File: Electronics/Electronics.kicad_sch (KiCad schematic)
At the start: 20 parts, among them J1 Barrel_Jack, M1 Fan_4pin, Q1 PN2222A, Q2 PN2222A, Q3 PN2222A, SW1 MOTOR_DECREASE, SW2 MOTOR_INCREASE, SW3 CYCLE_COLOR, SW4 CYCLE_MODE, U1 ESP32-DevKitC

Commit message: Updated schematic. Working on footprints. Need to add new DevKit Symbol to schematic
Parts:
- removed U1: ESP32-DevKitC, PCM_Espressif:ESP32-DevKitC, symbol PCM_Espressif:ESP32-DevKitC
- added R10, R11: 10K, symbol Device:R
- added R9: 100, symbol Device:R
- added SW5: SW_Wuerth_450301014042, Button_Switch_THT:SW_Slide-03_Wuerth-WS-SLTV_10x2.5x6.4_P2.54mm, symbol Switch:SW_Wuerth_450301014042
- added U1: ~, symbol Custom_Symbols:ESP-32S-Dev-Board
- added U3: ESP32-DEVKIT-V1, ESP32-DEVKIT-V1:MODULE_ESP32_DEVKIT_V1, symbol ESP_DEVKITV1:ESP32-DEVKIT-V1
- D1: footprint (none) -> Connector:FanPinHeader_1x04_P2.54mm_Vertical
- D2: footprint (none) -> LED_THT:LED_D5.0mm
- J1: footprint Connector_BarrelJack:BarrelJack_SwitchcraftConxall_RAPC10U_Horizontal -> Connector_BarrelJack:BarrelJack_Wuerth_6941xx301002
- SW1, SW2, SW3, SW4: footprint (none) -> Button_Switch_THT:SW_PUSH_6mm
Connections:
- net GND: now also R9.2; no longer D2.1 (K), Q1.1 (E), Q2.1 (E), Q3.1 (E), U2.4 (GND)
- net at SW1.1, SW2.1, SW3.1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: now also U1.15 (Vin)
- net at SW2.4 (A): now also U1.7 (D33)
- net at D1.1 (A), M1.2 (+): now also SW5.3 (A); no longer U2.1 (VIN)
- net at R7.2: now also U1.19 (D2)
- net at D1.3 (RK): now also Q3.3 (C); no longer Q1.3 (C)
- net at D1.4 (BK): now also Q1.3 (C); no longer Q3.3 (C)
- net at R5.2: now also U1.23 (D5)
- net at R6.2: now also U1.20 (D4)
- net at SW3.3 (K): now also U1.4 (D34)
- net at SW4.4 (A): now also U1.5 (D35)
- net at SW1.3 (K): now also U1.6 (D32)
- new net: D2.1 (K), R9.1
- new net: R10.1, R11.1, U1.14 (gnd), U2.4 (GND)
- new net: R11.2, U1.3 (VN)
- new net: SW5.2 (C), U2.1 (VIN)
- new net: R10.2, U1.2 (VP)
- new net: U3.2 (GND), U3.29 (GND)
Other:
- moved on the sheet: D2, R1, R2, R3, R4, SW1, SW2, SW3, SW4

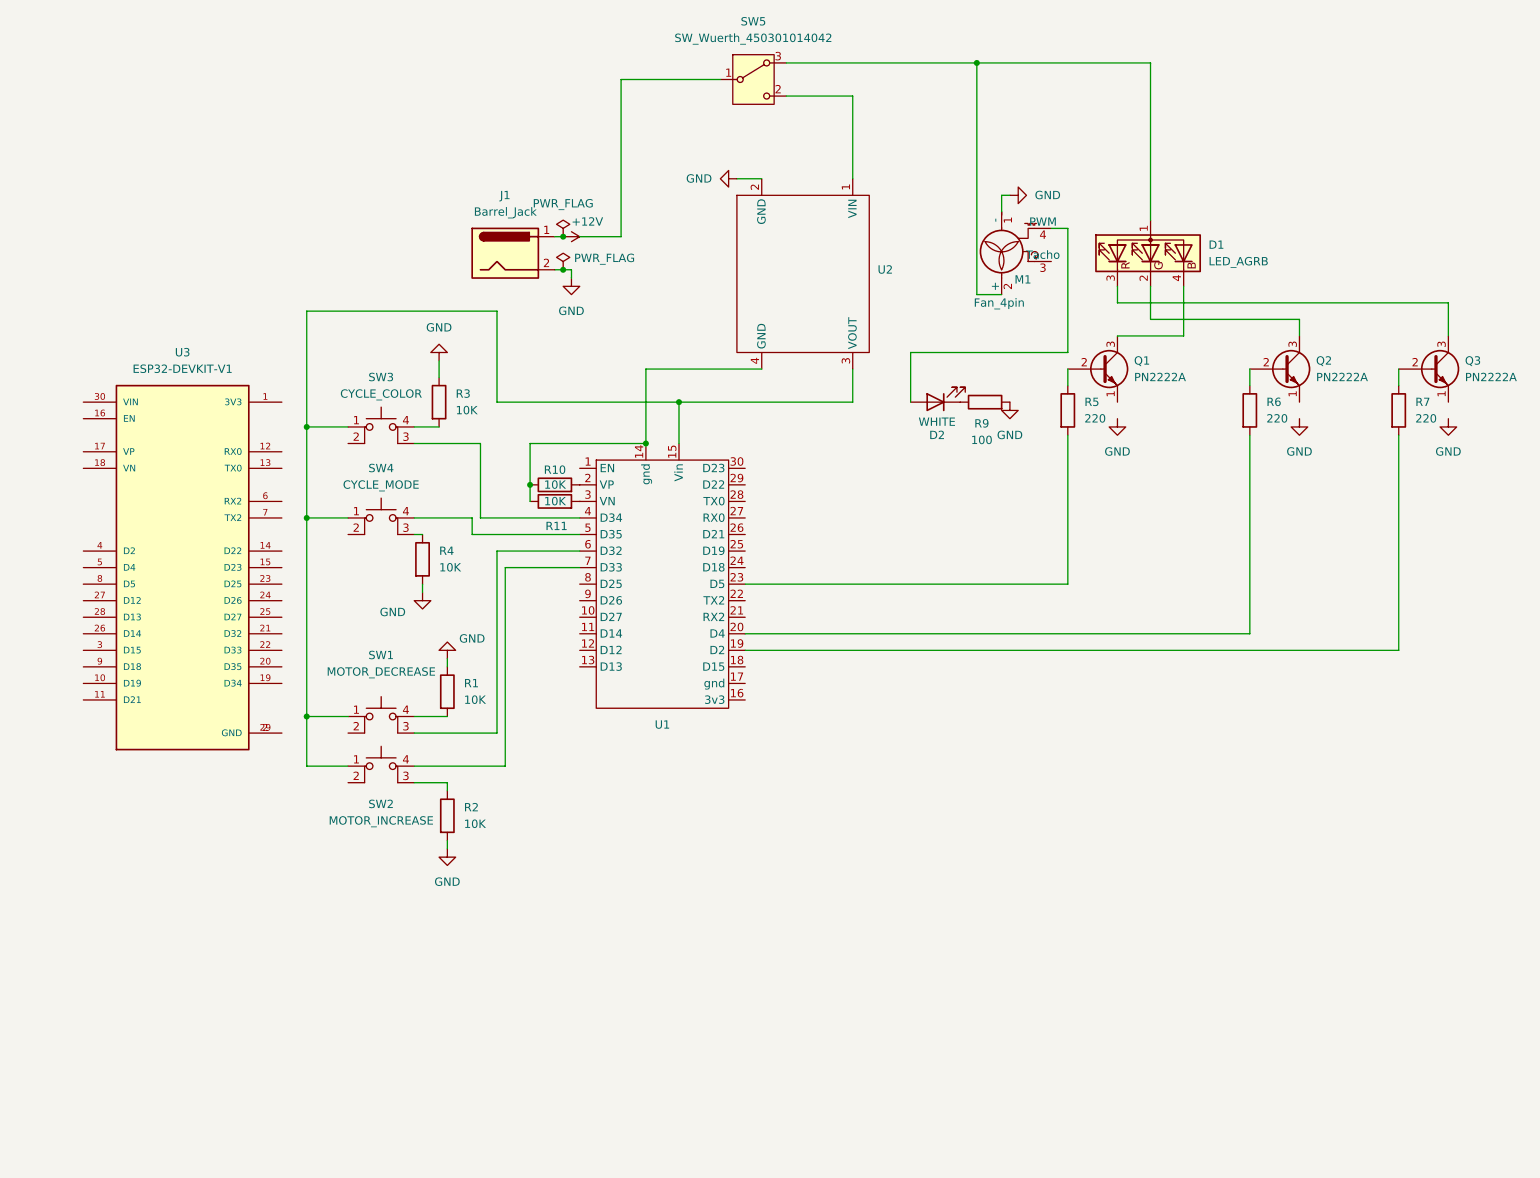
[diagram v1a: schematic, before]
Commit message: Began PCB design. Updated Footprints. Added Indication LEDs
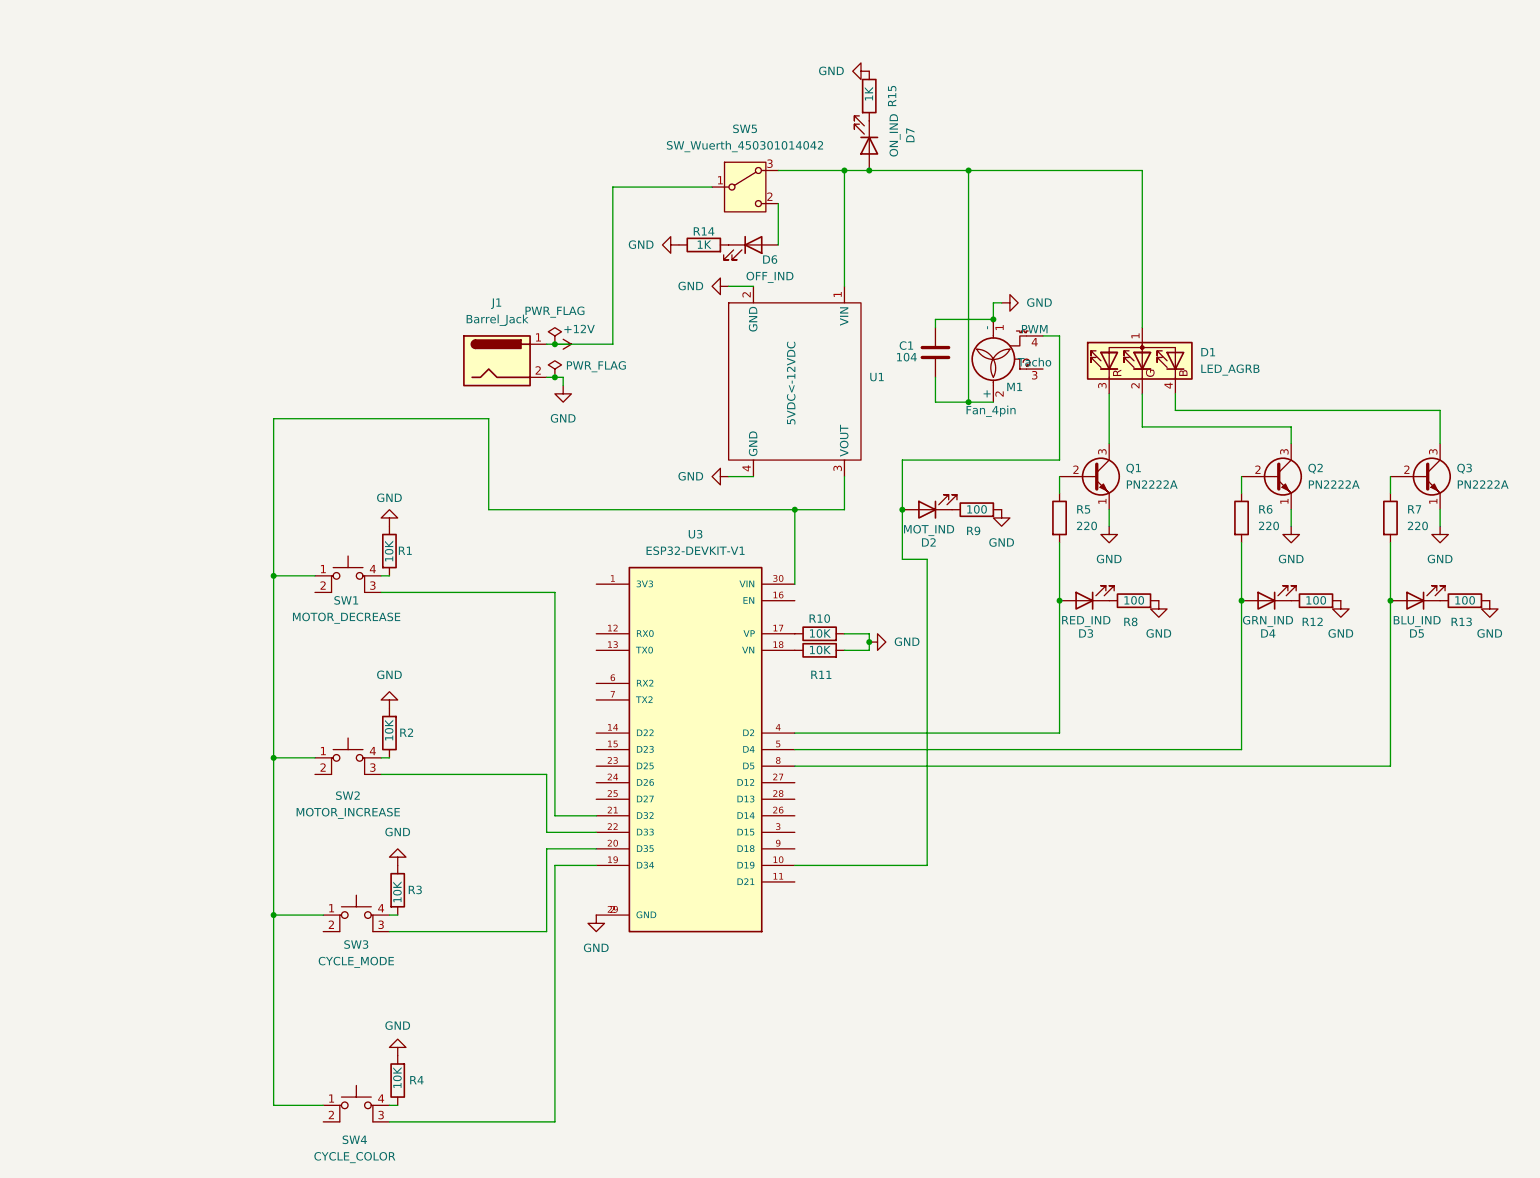
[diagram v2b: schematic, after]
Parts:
- removed U1: ~, symbol Custom_Symbols:ESP-32S-Dev-Board
- removed U2: ~, symbol Custom_Symbols:Buck_Converter
- added C1: 104, Capacitor_THT:C_Disc_D5.0mm_W2.5mm_P5.00mm, symbol Device:C
- added D3: RED_IND, LED_SMD:LED_1206_3216Metric_Pad1.42x1.75mm_HandSolder, symbol Device:LED
- added D4: GRN_IND, LED_SMD:LED_1206_3216Metric_Pad1.42x1.75mm_HandSolder, symbol Device:LED
- added D5: BLU_IND, LED_SMD:LED_1206_3216Metric_Pad1.42x1.75mm_HandSolder, symbol Device:LED
- added D6: OFF_IND, LED_SMD:LED_1206_3216Metric_Pad1.42x1.75mm_HandSolder, symbol Device:LED
- added D7: ON_IND, LED_SMD:LED_1206_3216Metric_Pad1.42x1.75mm_HandSolder, symbol Device:LED
- added R12, R13, R8: 100, Resistor_SMD:R_1206_3216Metric_Pad1.30x1.75mm_HandSolder, symbol Device:R
- added R14, R15: 1K, Resistor_SMD:R_1206_3216Metric_Pad1.30x1.75mm_HandSolder, symbol Device:R
- added U1: 5VDC<-12VDC, Custom:Buck_Converter, symbol Josh_Symbol:Buck_Converter
- D2: value WHITE -> MOT_IND; footprint LED_THT:LED_D5.0mm -> LED_SMD:LED_1206_3216Metric_Pad1.42x1.75mm_HandSolder
- R1, R10, R11, R2, R3, R4, R5, R6, R7, R9: footprint (none) -> Resistor_SMD:R_1206_3216Metric_Pad1.30x1.75mm_HandSolder
- SW1, SW2: footprint Button_Switch_THT:SW_PUSH_6mm -> Custom:SW_PUSH_6mm
- SW3: value CYCLE_COLOR -> CYCLE_MODE; footprint Button_Switch_THT:SW_PUSH_6mm -> Custom:SW_PUSH_6mm
- SW4: value CYCLE_MODE -> CYCLE_COLOR; footprint Button_Switch_THT:SW_PUSH_6mm -> Custom:SW_PUSH_6mm
- U3: footprint ESP32-DEVKIT-V1:MODULE_ESP32_DEVKIT_V1 -> ESP32_DEVKITV1:MODULE_ESP32_DEVKIT_V1
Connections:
- net +12V: now also SW5.1 (B)
- net GND: now also Q1.1 (E), Q2.1 (E), Q3.1 (E), R10.2, R11.2, U3.2 (GND), U3.29 (GND), C1.1, R12.2, R13.2, R14.1, R15.1, R8.2, U1.2 (GND), U1.4 (GND)
- net at R11.1: now also U3.18 (VN); no longer R10.1
- net at SW1.1, SW2.1, SW3.1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: now also U3.30 (VIN), U1.3 (VOUT)
- net at SW2.3 (K): now also U3.22 (D33); no longer R2.1
- net at SW2.4 (A): now also R2.1
- net at D1.1 (A), M1.2 (+), SW5.3 (A): now also C1.2, D7.2 (A), U1.1 (VIN)
- net at D2.2 (A), M1.4 (PWM): now also U3.10 (D19)
- net at R7.2: now also U3.8 (D5), D5.2 (A)
- net at D1.3 (RK): now also Q1.3 (C); no longer Q3.3 (C)
- net at D1.4 (BK): now also Q3.3 (C); no longer Q1.3 (C)
- net at SW5.2 (C): now also D6.2 (A)
- net at R5.2: now also U3.4 (D2), D3.2 (A)
- net at R4.1: now also SW4.4 (A); no longer SW4.3 (K)
- net at R6.2: now also U3.5 (D4), D4.2 (A)
- net at SW1.3 (K): now also U3.21 (D32)
- net at SW3.3 (K): now also U3.20 (D35)
- net at U3.17 (VP): now also R10.1
- net at U3.19 (D34): now also SW4.3 (K)
- new net: D5.1 (K), R13.1
- new net: D7.1 (K), R15.2
- new net: D3.1 (K), R8.1
- new net: D4.1 (K), R12.1
- new net: D6.1 (K), R14.2
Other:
- moved on the sheet: D1, D2, J1, M1, Q1, Q2, Q3, R1, R10, R11, R2, R3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

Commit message: Finalized. Awaiting PCB Production
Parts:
- added H1, H2, H3, H4, H5: MountingHole, MountingHole:MountingHole_3.2mm_M3, symbol Mechanical:MountingHole
- D1: footprint Connector:FanPinHeader_1x04_P2.54mm_Vertical -> Connector_PinHeader_2.54mm:PinHeader_1x04_P2.54mm_Vertical
- U3: footprint ESP32_DEVKITV1:MODULE_ESP32_DEVKIT_V1 -> Custom:MODULE_ESP32_DEVKIT_V1_NO_MOUNT
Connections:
- net at SW2.2: now also SW1.2, SW3.2, SW4.2, U1.3 (VOUT), U3.30 (VIN)
- net GND renamed GND_LOW
- net GND_LOW: no longer C1.1, J1.2, M1.1 (-), Q1.1 (E), Q2.1 (E), Q3.1 (E), R14.1, R15.1, U1.2 (GND)
- new net GND_HIGH: C1.1, J1.2, M1.1 (-), Q1.1 (E), Q2.1 (E), Q3.1 (E), R14.1, R15.1, U1.2 (GND)
- now unconnected: SW1.1, SW2.1, SW3.1, SW4.1
